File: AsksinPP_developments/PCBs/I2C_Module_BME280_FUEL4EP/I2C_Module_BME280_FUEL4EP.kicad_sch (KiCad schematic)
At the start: 12 parts, among them J1 Conn_01x04, J2 Conn_01x04, U1 BME280

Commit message: PCBs: I2C_Module_BME280_FUEL4EP and I2C_Module_BME680_FUEL4EP: updated LCSC numberss for assembly at JLCPCB
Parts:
- C1: LCSC (none) -> C19666; TYPE (none) -> 0603
- C3, C4: LCSC (none) -> C14663; TYPE (none) -> 0603
- R1, R2: LCSC (none) -> C25900; TYPE (none) -> 0402
- R3: LCSC (none) -> C25744; TYPE (none) -> 0402
- U1: LCSC (none) -> C92489; TYPE (none) -> LGA-8
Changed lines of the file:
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@@
       (effects (font (size 1.27 1.27)) hide)
+    )
+    (property "LCSC" "C25900" (id 4) (at 151.765 120.65 0)
+      (effects (font (size 1.524 1.524)) hide)
+    )
+    (property "TYPE" "0402" (id 5) (at 151.765 120.65 0)
+      (effects (font (size 1.524 1.524)) hide)
     )
     (pin "1")
@@
       (effects (font (size 1.27 1.27)) hide)
     )
+    (property "LCSC" "C14663" (id 4) (at 137.795 54.61 0)
+      (effects (font (size 0 0)) hide)
+    )
+    (property "TYPE" "0603" (id 5) (at 137.795 54.61 0)
+      (effects (font (size 1.524 1.524)) hide)
+    )
     (pin "1")
     (pin "2")
@@
       (effects (font (size 1.27 1.27)) hide)
     )
+    (property "LCSC" "C25744" (id 4) (at 173.355 55.88 0)
+      (effects (font (size 1.524 1.524)) hide)
+    )
+    (property "TYPE" "0402" (id 5) (at 173.355 55.88 0)
+      (effects (font (size 1.524 1.524)) hide)
+    )
     (pin "1")
     (pin "2")
@@
     (property "Datasheet" "https://ae-bst.resource.bosch.com/media/_tech/media/datasheets/BST-BME280-DS002.pdf" (id 3) (at 130.175 87.63 0)
       (effects (font (size 1.27 1.27)) hide)
+    )
+    (property "LCSC" "C92489" (id 4) (at 130.175 82.55 0)
+      (effects (font (size 1.524 1.524)) hide)
+    )
+    (property "TYPE" "LGA-8" (id 5) (at 130.175 82.55 0)
+      (effects (font (size 1.524 1.524)) hide)
     )
     (pin "1")
@@
       (effects (font (size 1.27 1.27)) hide)
     )
+    (property "LCSC" "C19666" (id 4) (at 79.375 130.175 90)
+      (effects (font (size 1.524 1.524)) hide)
+    )
+    (property "TYPE" "0603" (id 5) (at 79.375 130.175 90)
+      (effects (font (size 1.524 1.524)) hide)
+    )
     (pin "1")
     (pin "2")
@@
     (property "Datasheet" "~" (id 3) (at 121.285 54.61 0)
       (effects (font (size 1.27 1.27)) hide)
+    )
+    (property "LCSC" "C14663" (id 4) (at 121.285 54.61 0)
+      (effects (font (size 0 0)) hide)
+    )
+    (property "TYPE" "0603" (id 5) (at 121.285 54.61 0)
+      (effects (font (size 1.524 1.524)) hide)
     )
     (pin "1")
@@
       (effects (font (size 1.27 1.27)) hide)
     )
-    (pin "1")
+    (property "LCSC" "C25900" (id 4) (at 158.115 120.65 0)
+      (effects (font (size 1.524 1.524)) hide)
+    )
+    (property "TYPE" "0402" (id 5) (at 158.115 120.65 0)
+      (effects (font (size 1.524 1.524)) hide)
+    )
+    (pin "1")

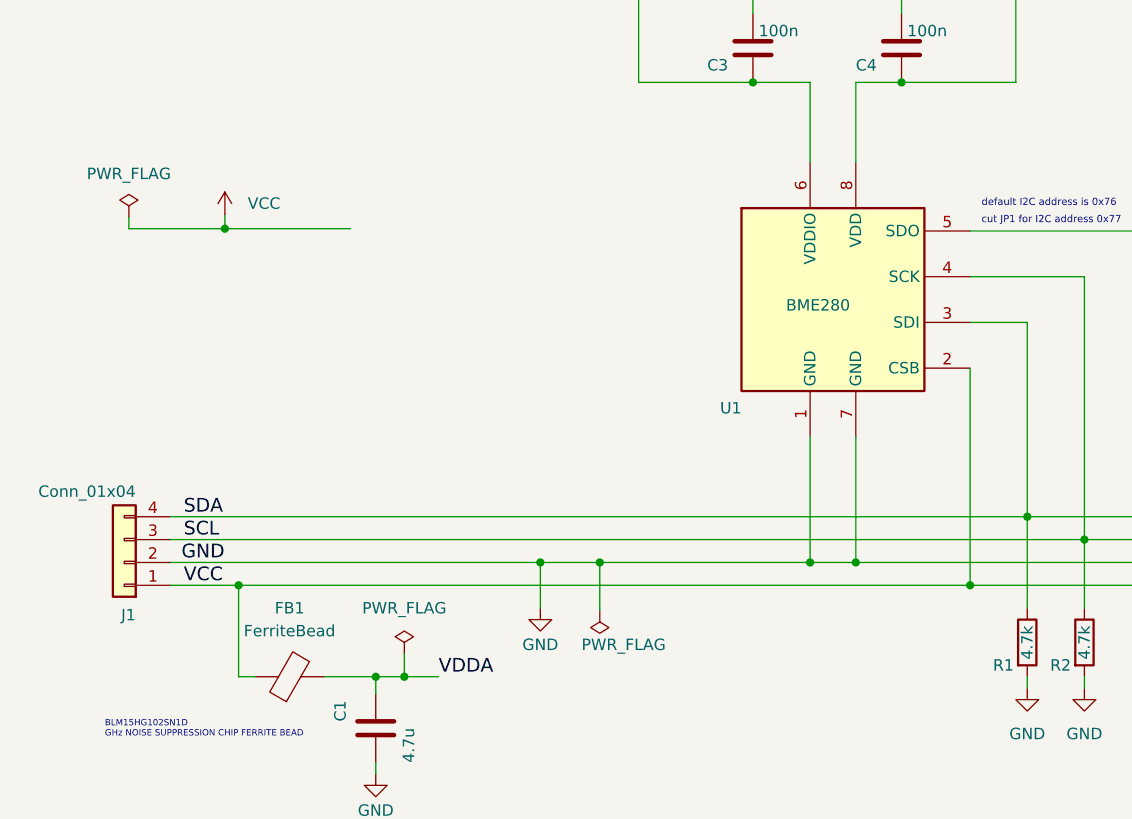
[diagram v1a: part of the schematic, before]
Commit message: PCBs: fix of some project specific KiCAD library paths for portability and missing PWR_FLGs for VCC in some schematics
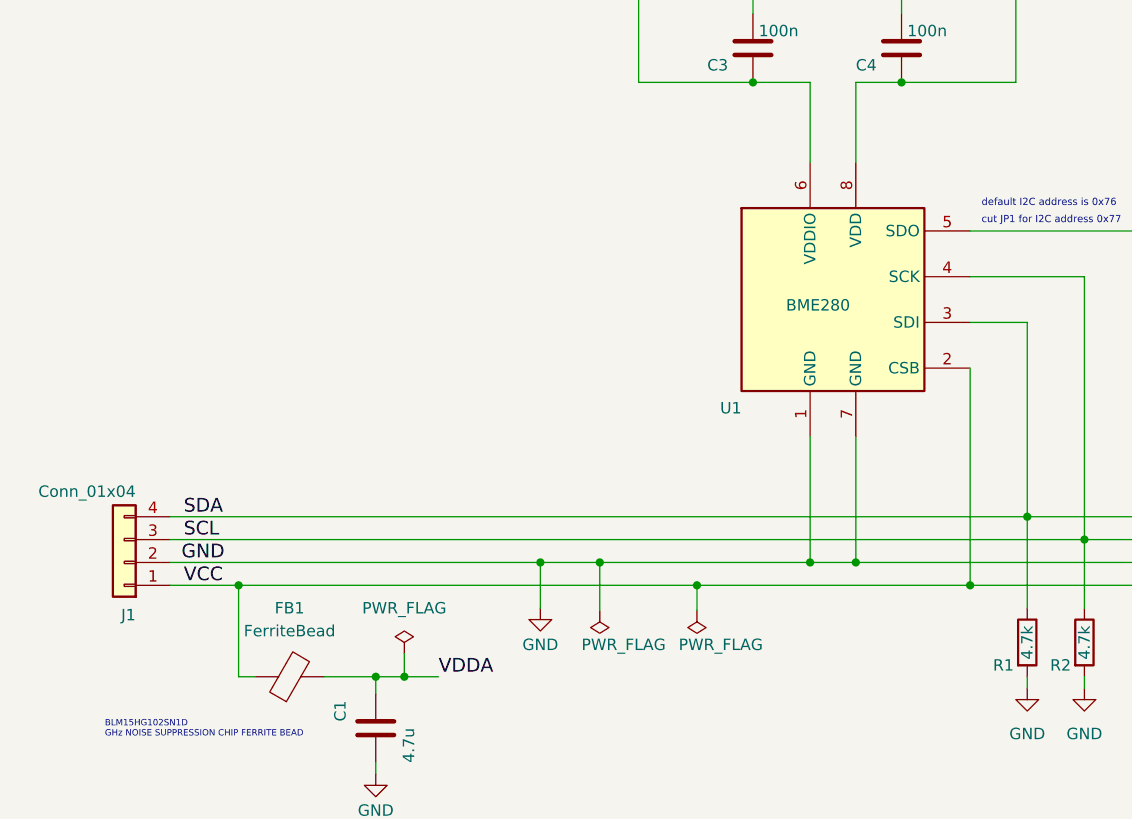
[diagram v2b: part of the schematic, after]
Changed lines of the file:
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@@
   (title_block
     (title "I2C_Module_BME280_FUEL4EP")
-    (date "2023-09-07")
-    (rev "1.0")
+    (date "2024-01-14")
+    (rev "1.1")
     (company "FUEL4EP")
     (comment 1 "fitting to  HB-UNI-SEN-BATT_ATMega1284P_E07-868MS10_FUEL4EP")
@@
   (junction (at 64.135 114.3) (diameter 0) (color 0 0 0 0)
   )
+  (junction (at 115.062 114.3) (diameter 0) (color 0 0 0 0)
+  )
   (junction (at 132.715 111.76) (diameter 0) (color 0 0 0 0)
   )
-  (junction (at 62.611 74.676) (diameter 0) (color 0 0 0 0)
-  )
   (junction (at 137.795 58.42) (diameter 0) (color 0 0 0 0)
   )
@@
     (stroke (width 0) (type default) (color 0 0 0 0))
   )
-  (wire (pts (xy 51.943 74.676) (xy 51.943 73.406))
-    (stroke (width 0) (type default) (color 0 0 0 0))
-  )
   (wire (pts (xy 121.285 48.26) (xy 121.285 50.8))
     (stroke (width 0) (type default) (color 0 0 0 0))
@@
     (stroke (width 0) (type default) (color 0 0 0 0))
   )
-  (wire (pts (xy 62.611 74.676) (xy 51.943 74.676))
+  (wire (pts (xy 115.062 117.094) (xy 115.062 114.3))
     (stroke (width 0) (type default) (color 0 0 0 0))
   )
@@
     (stroke (width 0) (type default) (color 0 0 0 0))
   )
-  (wire (pts (xy 62.611 74.676) (xy 62.611 73.152))
-    (stroke (width 0) (type default) (color 0 0 0 0))
-  )
   (wire (pts (xy 108.585 58.42) (xy 121.285 58.42))
     (stroke (width 0) (type default) (color 0 0 0 0))
   )
-  (wire (pts (xy 64.135 114.3) (xy 145.415 114.3))
+  (wire (pts (xy 64.135 114.3) (xy 115.062 114.3))
     (stroke (width 0) (type default) (color 0 0 0 0))
   )
@@
     (stroke (width 0) (type default) (color 0 0 0 0))
   )
-  (wire (pts (xy 62.611 74.676) (xy 76.581 74.676))
-    (stroke (width 0) (type default) (color 0 0 0 0))
-  )
   (wire (pts (xy 56.515 111.76) (xy 97.663 111.76))
     (stroke (width 0) (type default) (color 0 0 0 0))
@@
   )
   (wire (pts (xy 127.635 97.79) (xy 127.635 111.76))
+    (stroke (width 0) (type default) (color 0 0 0 0))
+  )
+  (wire (pts (xy 115.062 114.3) (xy 145.415 114.3))
     (stroke (width 0) (type default) (color 0 0 0 0))
   )
@@
     (pin "8")
   )
-  (symbol (lib_id "power:VCC") (at 62.611 73.152 0) (unit 1)
-    (in_bom yes) (on_board yes) (fields_autoplaced)
-    (property "Reference" "#PWR01" (id 0) (at 62.611 76.962 0)
-      (effects (font (size 1.27 1.27)) hide)
-    )
-    (property "Value" "VCC" (id 1) (at 65.151 71.8819 0)
-      (effects (font (size 1.27 1.27)) (justify left))
-    )
-    (property "Footprint" "" (id 2) (at 62.611 73.152 0)
-      (effects (font (size 1.27 1.27)) hide)
-    )
-    (property "Datasheet" "" (id 3) (at 62.611 73.152 0)
+  (symbol (lib_id "power:PWR_FLAG") (at 115.062 117.094 180) (unit 1)
+    (in_bom yes) (on_board yes)
+    (property "Reference" "#FLG0102" (id 0) (at 115.062 118.999 0)
+      (effects (font (size 1.27 1.27)) hide)
+    )
+    (property "Value" "PWR_FLAG" (id 1) (at 113.03 120.904 0)
+      (effects (font (size 1.27 1.27)) (justify right))
+    )
+    (property "Footprint" "" (id 2) (at 115.062 117.094 0)
+      (effects (font (size 1.27 1.27)) hide)
+    )
+    (property "Datasheet" "~" (id 3) (at 115.062 117.094 0)
       (effects (font (size 1.27 1.27)) hide)
     )
@@
     (pin "1")
   )
-  (symbol (lib_id "power:PWR_FLAG") (at 51.943 73.406 0) (unit 1)
-    (in_bom yes) (on_board yes) (fields_autoplaced)
-    (property "Reference" "#FLG01" (id 0) (at 51.943 71.501 0)
-      (effects (font (size 1.27 1.27)) hide)
-    )
-    (property "Value" "PWR_FLAG" (id 1) (at 51.943 68.58 0))
-    (property "Footprint" "" (id 2) (at 51.943 73.406 0)
-      (effects (font (size 1.27 1.27)) hide)
-    )
-    (property "Datasheet" "~" (id 3) (at 51.943 73.406 0)
-      (effects (font (size 1.27 1.27)) hide)
-    )
-    (pin "1")
-  )
   (symbol (lib_id "power:PWR_FLAG") (at 104.267 117.094 180) (unit 1)
     (in_bom yes) (on_board yes)
@@
   )
   (symbol_instances
-    (path "/accbd0c3-e588-4a03-8c25-5dc64064deb9"
-      (reference "#FLG01") (unit 1) (value "PWR_FLAG") (footprint "")
-    )
     (path "/b998681a-aa50-4b75-bf22-d9fbe42fce6f"
       (reference "#FLG02") (unit 1) (value "PWR_FLAG") (footprint "")
@@
       (reference "#FLG0101") (unit 1) (value "PWR_FLAG") (footprint "")
     )
-    (path "/71fc455e-be46-44e1-9ad6-6659dc653656"
-      (reference "#PWR01") (unit 1) (value "VCC") (footprint "")
+    (path "/6e0adbac-7b56-43b0-a1a6-f4a285e4aa76"
+      (reference "#FLG0102") (unit 1) (value "PWR_FLAG") (footprint "")
     )
     (path "/2fb280af-9352-43f7-93d8-89326fb5dc6f"

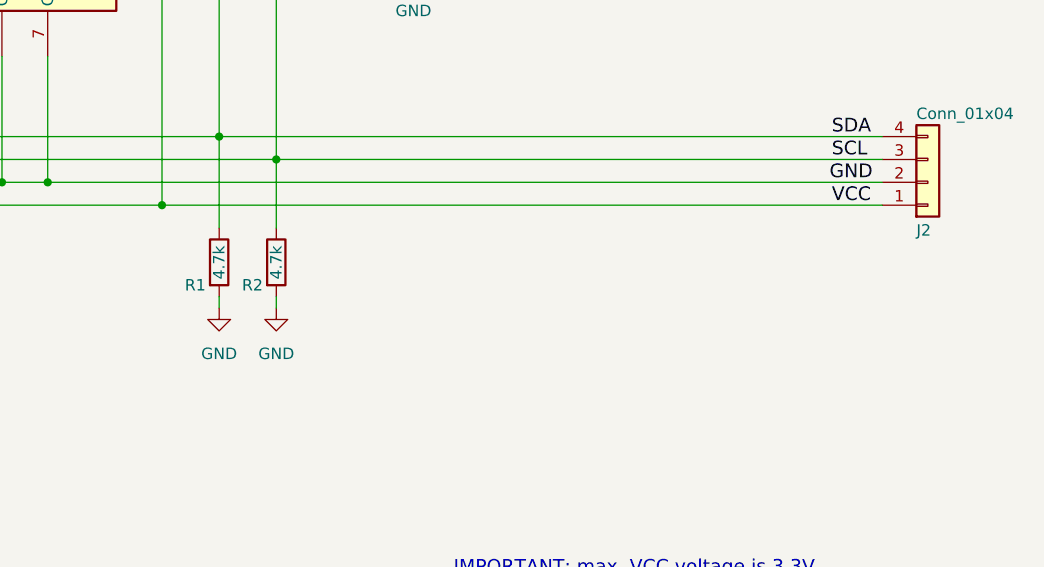
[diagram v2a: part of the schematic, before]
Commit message: PCBs: fix of I2C Pull-up resistors that were wrongly tied to GND
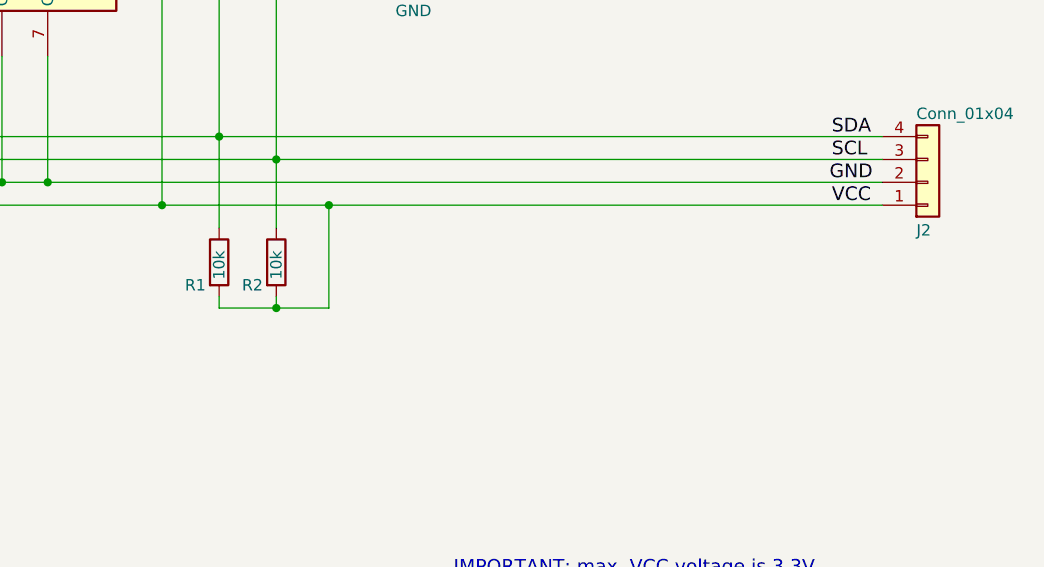
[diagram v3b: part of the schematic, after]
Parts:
- R1, R2: value 4.7k -> 10k; LCSC C25900 -> C25744
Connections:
- net GND: no longer R1.2, R2.2
- net VCC: now also R1.2, R2.2
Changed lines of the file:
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@@
   (title_block
     (title "I2C_Module_BME280_FUEL4EP")
-    (date "2024-01-14")
-    (rev "1.1")
+    (date "2024-02-08")
+    (rev "1.3")
     (company "FUEL4EP")
     (comment 1 "fitting to  HB-UNI-SEN-BATT_ATMega1284P_E07-868MS10_FUEL4EP")
@@
   (junction (at 137.795 58.42) (diameter 0) (color 0 0 0 0)
   )
+  (junction (at 158.115 125.73) (diameter 0) (color 0 0 0 0)
+  )
   (junction (at 79.375 124.46) (diameter 0) (color 0 0 0 0)
   )
@@
   (junction (at 145.415 114.3) (diameter 0) (color 0 0 0 0)
   )
+  (junction (at 163.957 114.3) (diameter 0) (color 0 0 0 0)
+  )
   (junction (at 82.55 124.46) (diameter 0) (color 0 0 0 0)
   )
@@
     (stroke (width 0) (type default) (color 0 0 0 0))
   )
+  (wire (pts (xy 158.115 125.73) (xy 163.957 125.73))
+    (stroke (width 0) (type default) (color 0 0 0 0))
+  )
   (wire (pts (xy 173.355 74.93) (xy 145.415 74.93))
     (stroke (width 0) (type default) (color 0 0 0 0))
@@
     (stroke (width 0) (type default) (color 0 0 0 0))
   )
+  (wire (pts (xy 163.957 125.73) (xy 163.957 114.3))
+    (stroke (width 0) (type default) (color 0 0 0 0))
+  )
   (wire (pts (xy 73.66 124.46) (xy 79.375 124.46))
     (stroke (width 0) (type default) (color 0 0 0 0))
@@
     (stroke (width 0) (type default) (color 0 0 0 0))
   )
-  (wire (pts (xy 145.415 114.3) (xy 225.425 114.3))
+  (wire (pts (xy 145.415 114.3) (xy 163.957 114.3))
+    (stroke (width 0) (type default) (color 0 0 0 0))
+  )
+  (wire (pts (xy 163.957 114.3) (xy 225.425 114.3))
+    (stroke (width 0) (type default) (color 0 0 0 0))
+  )
+  (wire (pts (xy 151.765 125.73) (xy 158.115 125.73))
     (stroke (width 0) (type default) (color 0 0 0 0))
   )
@@
       (effects (font (size 1.27 1.27)) (justify left))
     )
-    (property "Value" "4.7k" (id 1) (at 151.765 122.555 90)
+    (property "Value" "10k" (id 1) (at 151.765 122.555 90)
       (effects (font (size 1.27 1.27)) (justify left))
     )
@@
       (effects (font (size 1.27 1.27)) hide)
     )
-    (property "LCSC" "C25900" (id 4) (at 151.765 120.65 0)
+    (property "LCSC" "C25744" (id 4) (at 151.765 120.65 0)
       (effects (font (size 1.524 1.524)) hide)
     )
@@
     )
     (property "Datasheet" "" (id 3) (at 121.285 48.26 0)
-      (effects (font (size 1.27 1.27)) hide)
-    )
-    (pin "1")
-  )
-  (symbol (lib_id "power:GND") (at 151.765 125.73 0) (unit 1)
-    (in_bom yes) (on_board yes) (fields_autoplaced)
-    (property "Reference" "#PWR07" (id 0) (at 151.765 132.08 0)
-      (effects (font (size 1.27 1.27)) hide)
-    )
-    (property "Value" "GND" (id 1) (at 151.765 130.81 0))
-    (property "Footprint" "" (id 2) (at 151.765 125.73 0)
-      (effects (font (size 1.27 1.27)) hide)
-    )
-    (property "Datasheet" "" (id 3) (at 151.765 125.73 0)
       (effects (font (size 1.27 1.27)) hide)
     )
@@
     (pin "1")
   )
-  (symbol (lib_id "power:GND") (at 158.115 125.73 0) (unit 1)
-    (in_bom yes) (on_board yes) (fields_autoplaced)
-    (property "Reference" "#PWR08" (id 0) (at 158.115 132.08 0)
-      (effects (font (size 1.27 1.27)) hide)
-    )
-    (property "Value" "GND" (id 1) (at 158.115 130.81 0))
-    (property "Footprint" "" (id 2) (at 158.115 125.73 0)
-      (effects (font (size 1.27 1.27)) hide)
-    )
-    (property "Datasheet" "" (id 3) (at 158.115 125.73 0)
-      (effects (font (size 1.27 1.27)) hide)
-    )
-    (pin "1")
-  )
   (symbol (lib_id "power:VDDA") (at 150.495 48.26 0) (unit 1)
     (in_bom yes) (on_board yes) (fields_autoplaced)
@@
       (effects (font (size 1.27 1.27)) (justify left))
     )
-    (property "Value" "4.7k" (id 1) (at 158.115 122.555 90)
+    (property "Value" "10k" (id 1) (at 158.115 122.555 90)
       (effects (font (size 1.27 1.27)) (justify left))
     )
@@
       (effects (font (size 1.27 1.27)) hide)
     )
-    (property "LCSC" "C25900" (id 4) (at 158.115 120.65 0)
+    (property "LCSC" "C25744" (id 4) (at 158.115 120.65 0)
       (effects (font (size 1.524 1.524)) hide)
     )
@@
       (reference "#PWR05") (unit 1) (value "GND") (footprint "")
     )
-    (path "/18542ab6-239f-4332-a70c-3c8551b285bb"
-      (reference "#PWR07") (unit 1) (value "GND") (footprint "")
-    )
-    (path "/d43541cc-8fb7-4c57-a7c8-5b5588c55acf"
-      (reference "#PWR08") (unit 1) (value "GND") (footprint "")
-    )
     (path "/3c4dcae3-942c-4516-aa17-b3223b1ea5e6"
       (reference "#PWR010") (unit 1) (value "GND") (footprint "")
@@
     )
     (path "/010452d5-e5f2-447e-a153-71da0dbec114"
-      (reference "R1") (unit 1) (value "4.7k") (footprint "Resistor_SMD:R_0402_1005Metric")
+      (reference "R1") (unit 1) (value "10k") (footprint "Resistor_SMD:R_0402_1005Metric")
     )
     (path "/f75dc7be-70bf-4119-8c06-195e1a960dd2"
-      (reference "R2") (unit 1) (value "4.7k") (footprint "Resistor_SMD:R_0402_1005Metric")
+      (reference "R2") (unit 1) (value "10k") (footprint "Resistor_SMD:R_0402_1005Metric")
     )
     (path "/55b96afd-ec19-4400-9134-cc56302d872a"
